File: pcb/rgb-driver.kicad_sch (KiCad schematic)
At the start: 7 parts, among them U8 IS31FL3193

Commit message: Revision E
- Resolve issues 1-11
- Add pdf of rev d schematic for easy comparison
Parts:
- C36: footprint Capacitor_SMD:C_0603_1608Metric -> Capacitor_SMD:C_0402_1005Metric
- R23, R24: value 4.7k -> 10k
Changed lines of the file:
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@@
 			)
 		)
-		(property "Value" "4.7k"
+		(property "Value" "10k"
 			(at 115.57 62.23 0)
 			(effects
@@
 			)
 		)
-		(property "Footprint" "Capacitor_SMD:C_0603_1608Metric"
+		(property "Footprint" "Capacitor_SMD:C_0402_1005Metric"
 			(at 134.3152 66.04 0)
 			(effects
@@
 			)
 		)
-		(property "Value" "4.7k"
+		(property "Value" "10k"
 			(at 115.57 83.82 0)
 			(effects

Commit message: Revision F Edits
- Reduce base capacitance
  - Reduce infill {width, gap}: {0.35, 1} -> {0.2, 1.2}
    - Equivalent to: 45.1% -> 26.5%
  - Entirely remove copper on 3rd (in2.Cu) layer
  - Reduce via count
- export rev e schematic to pdf
- put pdfs into manufacturing folder
- Fix 6mm tactile switch footprint
- Put gold under logo
- Increment schematic, pcb, and silkscreen revision to F
- Add labels to debug header
- Add 10k pull-up to tmc2130 enable pin
- Convert all symbols & footprints library aliases from "oe" to "open-ephys"
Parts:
- D1: footprint oe:SUNLED_PLCC4-INV_3.2x2.8x1.9mm -> open-ephys:SUNLED_PLCC4-INV_3.2x2.8x1.9mm
- U8: symbol oe:IS31FL3193 -> open-ephys:IS31FL3193
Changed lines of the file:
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@@
 			)
 		)
-		(property "Footprint" "oe:SUNLED_PLCC4-INV_3.2x2.8x1.9mm"
+		(property "Footprint" "open-ephys:SUNLED_PLCC4-INV_3.2x2.8x1.9mm"
 			(at 66.04 44.45 0)
 			(effects
@@
 	)
 	(symbol
-		(lib_id "oe:IS31FL3193")
+		(lib_id "open-ephys:IS31FL3193")
 		(at 88.9 69.85 0)
 		(unit 1)
@@
 			)
 		)
-		(property "Description" "3-CHANNEL LED DRIVER "
+		(property "Description" "3-CHANNEL LED DRIVER"
 			(at 88.9 69.85 0)
 			(effects

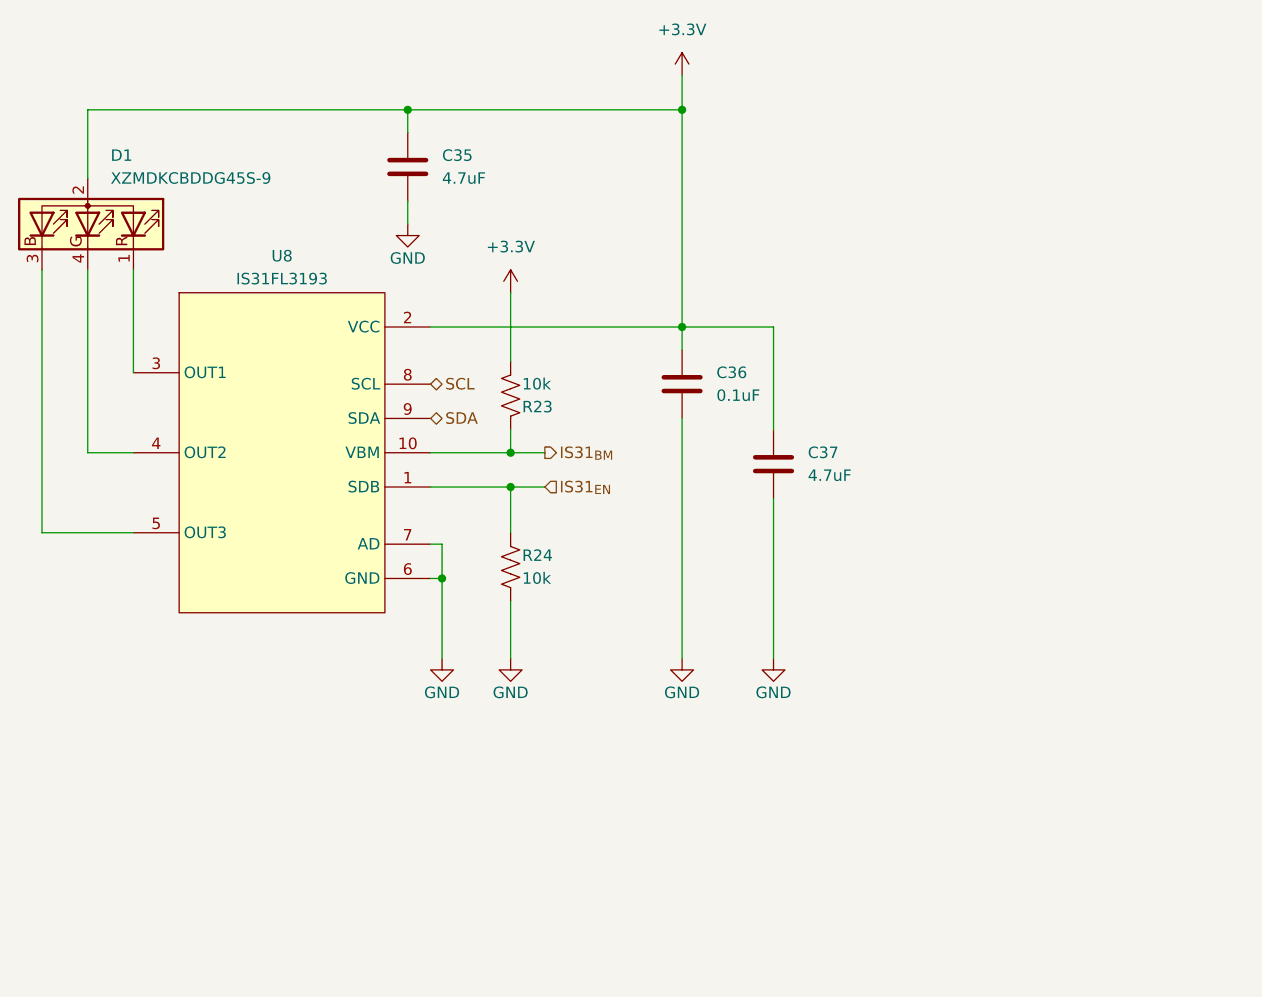
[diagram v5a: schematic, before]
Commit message: Final edits to rev G before fab
- Move USB connector twoards board edge by 1.5mm
- Make all silk text uniform
- Add required stackup and board characteristics to user.comments layer
- Redo 3.3V power routing to RP2040 (one power pin was not connected)
- Uniform schematic sheet size
- And many other small changes
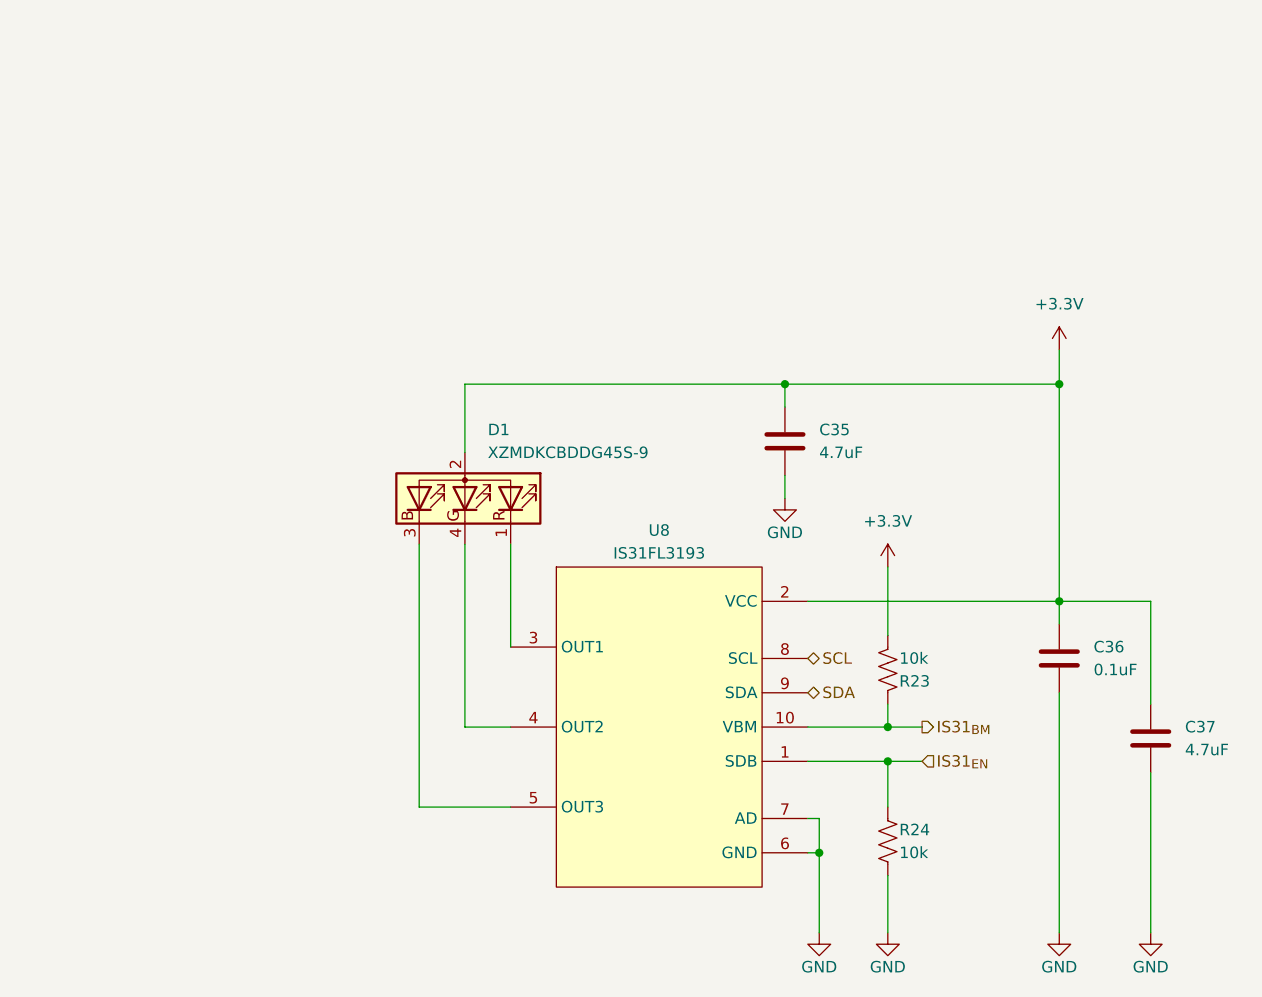
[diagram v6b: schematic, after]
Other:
- moved on the sheet: C35, C36, C37, D1, R23, R24, U8

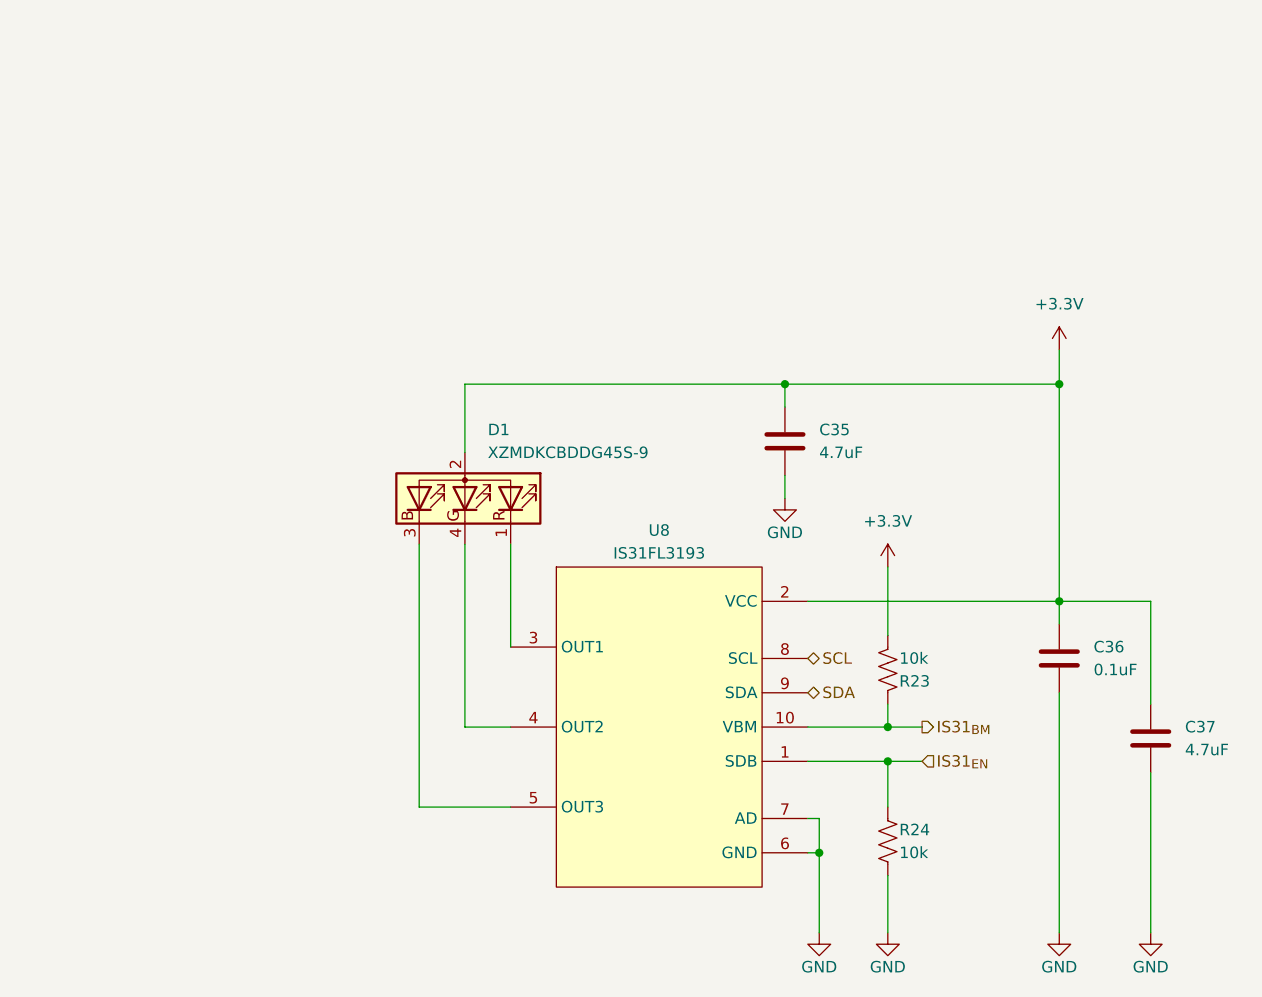
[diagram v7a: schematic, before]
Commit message: Small updates during review
- Schematic clarifications
- Update footprints to match library latest
- Small silkscreen and via positioning changes to support clean
  silkscreen
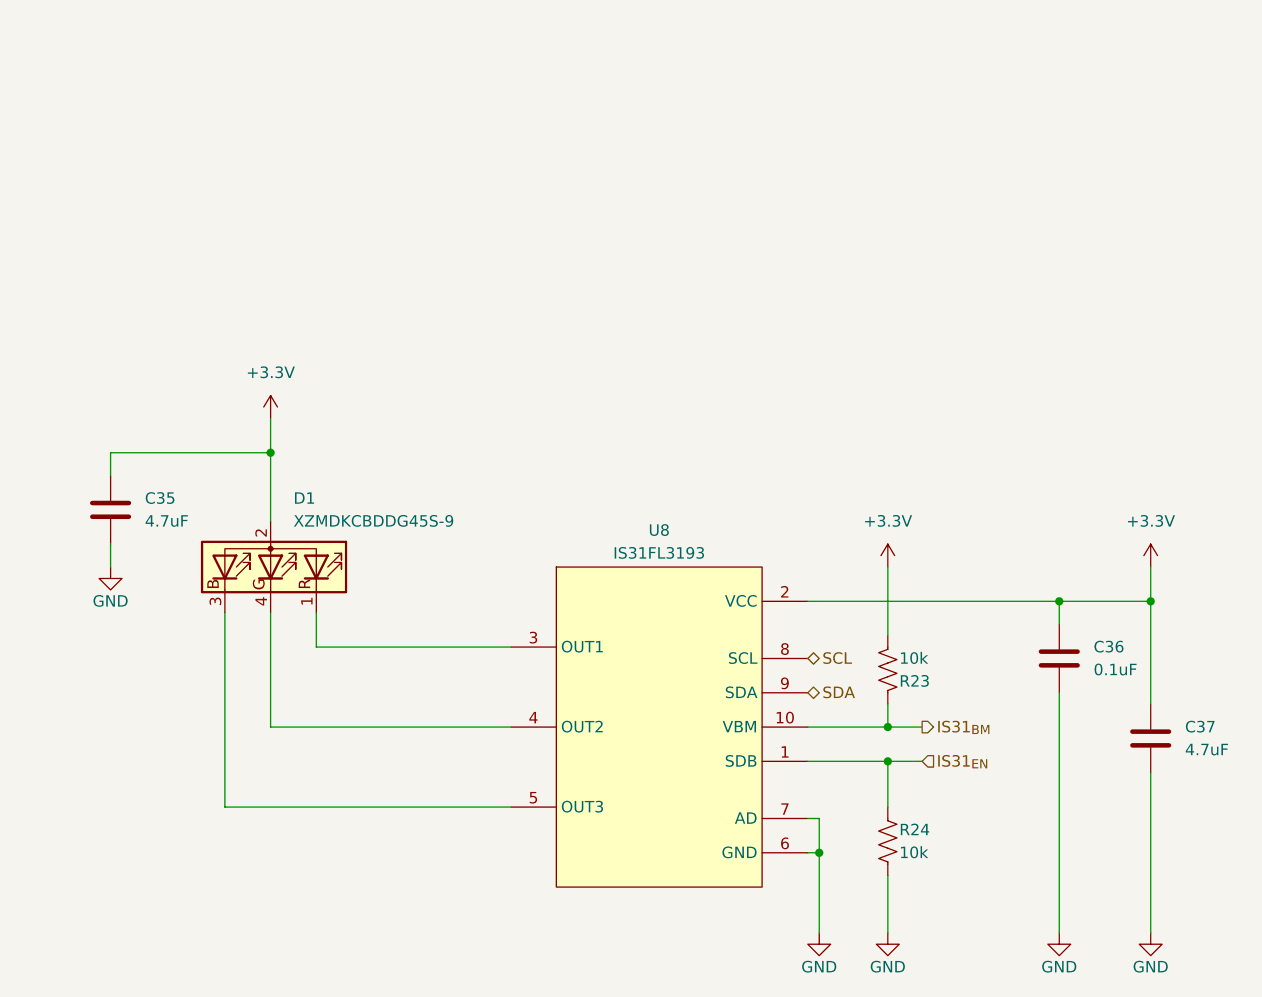
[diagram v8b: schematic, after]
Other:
- moved on the sheet: C35, D1
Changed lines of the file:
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@@
 	(title_block
 		(title "Open Ephys Commutator Controller")
-		(rev "G")
+		(rev "J")
 		(company "Open Ephys, Inc.")
 		(comment 1 "Cris Sharp")
@@
 	)
 	(junction
-		(at 175.26 62.23)
+		(at 87.63 69.85)
 		(diameter 0)
 		(color 0 0 0 0)
@@
 	)
 	(junction
+		(at 185.42 86.36)
+		(diameter 0)
+		(color 0 0 0 0)
+	)
+	(junction
 		(at 156.21 100.33)
 		(diameter 0)
@@
 		(color 0 0 0 0)
 	)
-	(junction
-		(at 144.78 62.23)
-		(diameter 0)
-		(color 0 0 0 0)
-	)
-	(wire
-		(pts
-			(xy 104.14 109.22) (xy 114.3 109.22)
+	(wire
+		(pts
+			(xy 82.55 109.22) (xy 114.3 109.22)
 		)
 		(stroke
@@
 	(wire
 		(pts
-			(xy 144.78 62.23) (xy 109.22 62.23)
-		)
-		(stroke
-			(width 0)
-			(type default)
-		)
-	)
-	(wire
-		(pts
 			(xy 148.59 114.3) (xy 148.59 123.19)
 		)
@@
 	(wire
 		(pts
-			(xy 144.78 62.23) (xy 144.78 64.77)
-		)
-		(stroke
-			(width 0)
-			(type default)
-		)
-	)
-	(wire
-		(pts
-			(xy 114.3 80.01) (xy 114.3 91.44)
-		)
-		(stroke
-			(width 0)
-			(type default)
-		)
-	)
-	(wire
-		(pts
-			(xy 109.22 100.33) (xy 114.3 100.33)
+			(xy 87.63 100.33) (xy 114.3 100.33)
 		)
 		(stroke
@@
 	(wire
 		(pts
+			(xy 69.85 80.01) (xy 69.85 82.55)
+		)
+		(stroke
+			(width 0)
+			(type default)
+		)
+	)
+	(wire
+		(pts
 			(xy 156.21 123.19) (xy 156.21 116.84)
 		)
@@
 	(wire
 		(pts
-			(xy 175.26 86.36) (xy 175.26 62.23)
-		)
-		(stroke
-			(width 0)
-			(type default)
-		)
-	)
-	(wire
-		(pts
-			(xy 144.78 62.23) (xy 175.26 62.23)
+			(xy 114.3 91.44) (xy 92.71 91.44)
+		)
+		(stroke
+			(width 0)
+			(type default)
+		)
+	)
+	(wire
+		(pts
+			(xy 185.42 82.55) (xy 185.42 86.36)
 		)
 		(stroke
@@
 	(wire
 		(pts
-			(xy 104.14 80.01) (xy 104.14 109.22)
+			(xy 82.55 87.63) (xy 82.55 109.22)
+		)
+		(stroke
+			(width 0)
+			(type default)
+		)
+	)
+	(wire
+		(pts
+			(xy 69.85 69.85) (xy 69.85 72.39)
+		)
+		(stroke
+			(width 0)
+			(type default)
+		)
+	)
+	(wire
+		(pts
+			(xy 87.63 69.85) (xy 69.85 69.85)
+		)
+		(stroke
+			(width 0)
+			(type default)
+		)
+	)
+	(wire
+		(pts
+			(xy 87.63 69.85) (xy 87.63 66.04)
 		)
 		(stroke
@@
 	(wire
 		(pts
-			(xy 175.26 62.23) (xy 175.26 58.42)
-		)
-		(stroke
-			(width 0)
-			(type default)
-		)
-	)
-	(wire
-		(pts
-			(xy 144.78 72.39) (xy 144.78 74.93)
-		)
-		(stroke
-			(width 0)
-			(type default)
-		)
-	)
-	(wire
-		(pts
 			(xy 185.42 105.41) (xy 185.42 123.19)
 		)
@@
 	(wire
 		(pts
-			(xy 109.22 62.23) (xy 109.22 69.85)
+			(xy 87.63 69.85) (xy 87.63 77.47)
 		)
 		(stroke
@@
 	(wire
 		(pts
-			(xy 109.22 80.01) (xy 109.22 100.33)
+			(xy 87.63 87.63) (xy 87.63 100.33)
 		)
 		(stroke
@@
 		(pts
 			(xy 175.26 86.36) (xy 175.26 88.9)
+		)
+		(stroke
+			(width 0)
+			(type default)
+		)
+	)
+	(wire
+		(pts
+			(xy 92.71 91.44) (xy 92.71 87.63)
 		)
 		(stroke
@@
 	(symbol
 		(lib_id "Device:C")
-		(at 144.78 68.58 0)
+		(at 69.85 76.2 0)
 		(unit 1)
 		(exclude_from_sim no)
@@
 		(dnp no)
 		(property "Reference" "C35"
-			(at 148.59 67.31 0)
+			(at 73.66 74.93 0)
 			(effects
 				(font
@@
 		)
 		(property "Value" "4.7uF"
-			(at 148.59 69.85 0)
+			(at 73.66 77.47 0)
 			(effects
 				(font
@@
 		)
 		(property "Footprint" "Capacitor_SMD:C_0805_2012Metric"
-			(at 145.7452 72.39 0)
+			(at 70.8152 80.01 0)
 			(effects
 				(font
@@
 		)
 		(property "Datasheet" "~"
-			(at 144.78 68.58 0)
+			(at 69.85 76.2 0)
 			(effects
 				(font
@@
 		)
 		(property "Description" "Unpolarized capacitor"
-			(at 144.78 68.58 0)
+			(at 69.85 76.2 0)
 			(effects
 				(font
@@
 	)
 	(symbol
+		(lib_id "power:+3.3V")
+		(at 87.63 66.04 0)
+		(unit 1)
+		(exclude_from_sim no)
+		(in_bom yes)
+		(on_board yes)
+		(dnp no)
+		(fields_autoplaced yes)
+		(property "Reference" "#PWR083"
+			(at 87.63 69.85 0)
+			(effects
+				(font
+					(size 1.27 1.27)
+				)
+				(hide yes)
+			)
+		)
+		(property "Value" "+3.3V"
+			(at 87.63 60.96 0)
+			(effects
+				(font
+					(size 1.27 1.27)
+				)
+			)
+		)
+		(property "Footprint" ""
+			(at 87.63 66.04 0)
+			(effects
+				(font
+					(size 1.27 1.27)
+				)
+				(hide yes)
+			)
+		)
+		(property "Datasheet" ""
+			(at 87.63 66.04 0)
+			(effects
+				(font
+					(size 1.27 1.27)
+				)
+				(hide yes)
+			)
+		)
+		(property "Description" "Power symbol creates a global label with name \"+3.3V\""
+			(at 87.63 66.04 0)
+			(effects
+				(font
+					(size 1.27 1.27)
+				)
+				(hide yes)
+			)
+		)
+		(pin "1"
+		)
+		(instances
+			(project "oe-commutator-controller"
+				(path "/f8e1d654-dc44-4fb2-953c-f5982945ff40/95463fce-2507-46a3-acfc-459accd379fb"
+					(reference "#PWR083")
+					(unit 1)
+				)
+			)
+		)
+	)
+	(symbol
 		(lib_id "power:GND")
 		(at 185.42 123.19 0)
@@
 	(symbol
 		(lib_id "Device:LED_RABG")
-		(at 109.22 74.93 270)
+		(at 87.63 82.55 270)
 		(mirror x)
 		(unit 1)
@@
 		(dnp no)
 		(property "Reference" "D1"
-			(at 111.76 67.31 90)
+			(at 90.17 74.93 90)
 			(effects
 				(font
@@
 		)
 		(property "Value" "XZMDKCBDDG45S-9"
-			(at 111.76 69.85 90)
+			(at 90.17 77.47 90)
 			(effects
 				(font
@@
 		)
 		(property "Footprint" "open-ephys:SUNLED_PLCC4-INV_3.2x2.8x1.9mm"
-			(at 107.95 74.93 0)
+			(at 86.36 82.55 0)
 			(effects
 				(font
@@
 		)
 		(property "Datasheet" "~"
-			(at 107.95 74.93 0)
+			(at 86.36 82.55 0)
 			(effects
 				(font
@@
 		)
 		(property "Description" "RGB LED, red/anode/blue/green"
-			(at 109.22 74.93 0)
+			(at 87.63 82.55 0)
 			(effects
 				(font
@@
 	(symbol
 		(lib_id "power:GND")
-		(at 144.78 74.93 0)
+		(at 69.85 82.55 0)
 		(unit 1)
 		(exclude_from_sim no)
@@
 		(dnp no)
 		(property "Reference" "#PWR070"
-			(at 144.78 81.28 0)
+			(at 69.85 88.9 0)
 			(effects
 				(font
@@
 		)
 		(property "Value" "GND"
-			(at 144.78 78.74 0)
+			(at 69.85 86.36 0)
 			(effects
 				(font
@@
 		)
 		(property "Footprint" ""
-			(at 144.78 74.93 0)
+			(at 69.85 82.55 0)
 			(effects
 				(font
@@
 		)
 		(property "Datasheet" ""
-			(at 144.78 74.93 0)
+			(at 69.85 82.55 0)
 			(effects
 				(font
@@
 		)
 		(property "Description" "Power symbol creates a global label with name \"GND\" , ground"
-			(at 144.78 74.93 0)
+			(at 69.85 82.55 0)
 			(effects
 				(font
@@
 	(symbol
 		(lib_id "power:+3.3V")
-		(at 175.26 58.42 0)
+		(at 185.42 82.55 0)
 		(unit 1)
 		(exclude_from_sim no)
@@
 		(fields_autoplaced yes)
 		(property "Reference" "#PWR069"
-			(at 175.26 62.23 0)
+			(at 185.42 86.36 0)
 			(effects
 				(font
@@
 		)
 		(property "Value" "+3.3V"
-			(at 175.26 53.34 0)
+			(at 185.42 77.47 0)
 			(effects
 				(font
@@
 		)
 		(property "Footprint" ""
-			(at 175.26 58.42 0)
+			(at 185.42 82.55 0)
 			(effects
 				(font
@@
 		)
 		(property "Datasheet" ""
-			(at 175.26 58.42 0)
+			(at 185.42 82.55 0)
 			(effects
 				(font
@@
 		)
 		(property "Description" "Power symbol creates a global label with name \"+3.3V\""
-			(at 175.26 58.42 0)
-			(effects
-				(font
+			(at 185.42 82.55 0)
+			(effects
+				(font
